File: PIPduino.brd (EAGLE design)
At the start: 46 x 46 mm, 41 parts, among them IC1 ATmega328P\, IC2 SPX1117, J1 ISP/SPI

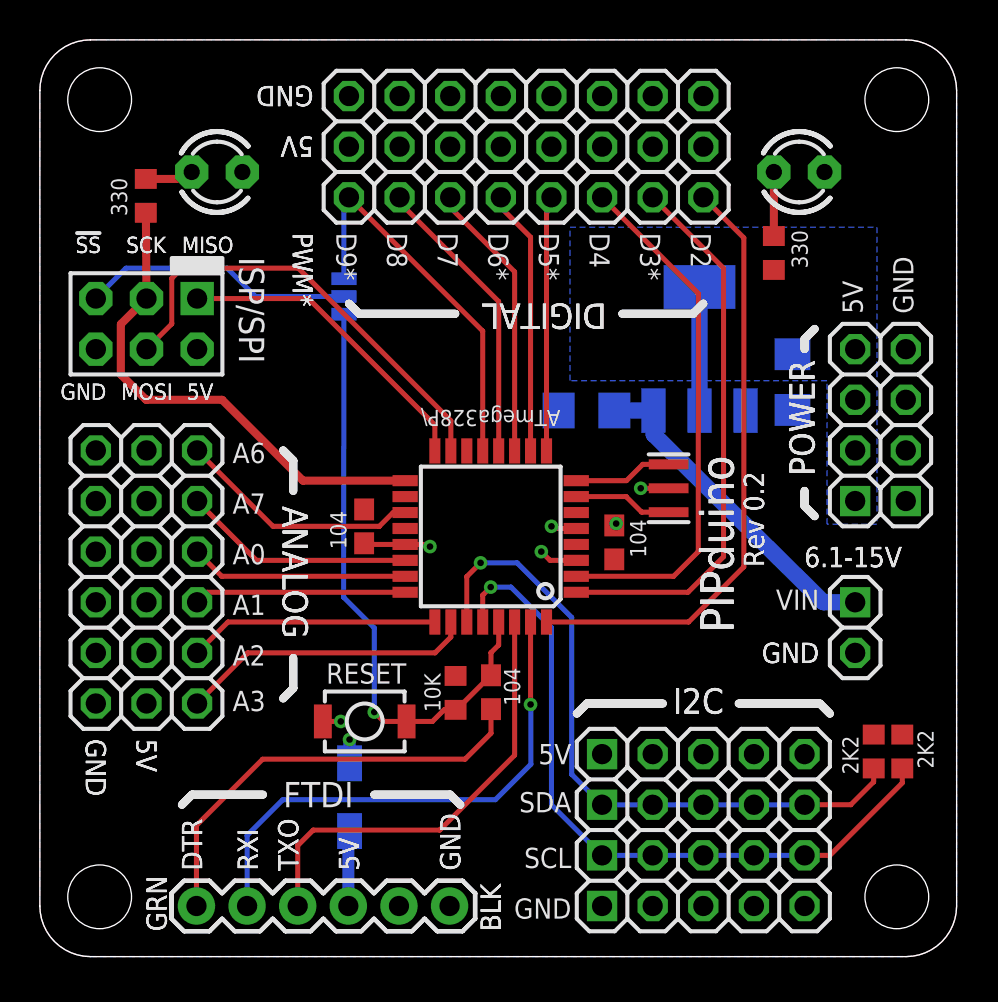
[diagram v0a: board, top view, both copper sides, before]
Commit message: Surrounded top screw holes with GND
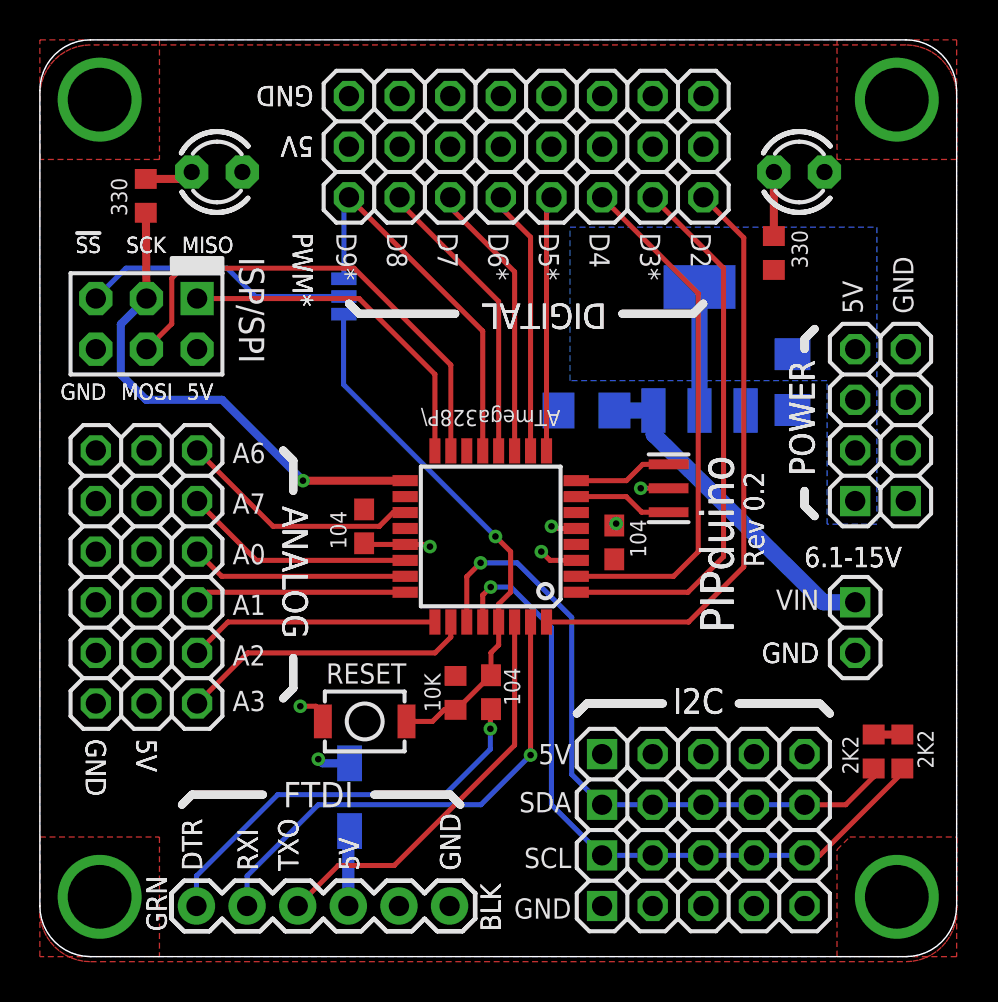
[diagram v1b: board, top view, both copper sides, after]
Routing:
- net !RESET: track 30.4 -> 27.2 mm
- net TXO: track 22.5 -> 20.4 mm
- net MOSI: track 23.0 -> 24.6 mm
- net 5V: track 7.76 -> 9.29 mm
- net MISO: track 15.9 -> 17.3 mm
- net RXI: track 26.4 -> 24.9 mm
- net N$15: track 22.0 -> 20.9 mm, vias 0 -> 1
- net GND: track 9.01 -> 9.81 mm, vias 6 -> 10
- net SCK: vias 0 -> 1
- added copper zone on layer 1, net GND

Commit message: Removed top 5V polygon, star pattern power, 106's on analog, 104 on aref, larger power traces, removed polygons on top mounting holes
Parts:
- added C6: 104, rcl:C0603
- added C7, C8: 106, rcl:C1206
- moved C5 2.08 mm to (29.0, 26.0), turned to 270 degrees
- moved C1 1.84 mm to (15.2, 23.1), turned to 180 degrees
- moved C3 0.60 mm to (29.4, 20.7), turned to 0 degrees
- moved C4 0.23 mm to (22.9, 13.2)
- moved R4 0.23 mm to (21.1, 13.2), turned to 270 degrees
- renumbered U$1 to X1
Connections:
- new net N$6: C6.1, IC1.20
- net 5V: now also C7.1, C8.1; no longer IC1.20
- net GND: now also C6.2, C7.2, C8.2
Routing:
- net 5V: track 9.29 -> 134.1 mm, vias 1 -> 5
- net N$6: track 0.00 -> 2.59 mm
- net !RESET: track 27.2 -> 27.9 mm
- net GND: track 9.81 -> 10.5 mm, vias 10 -> 12
- net A6: track 12.3 -> 11.8 mm, vias 0 -> 1
- net SCK: track 25.1 -> 25.4 mm, vias 1 -> 0
- removed copper zone on layer 1, net 5V
- removed copper zone on layer 1, net GND

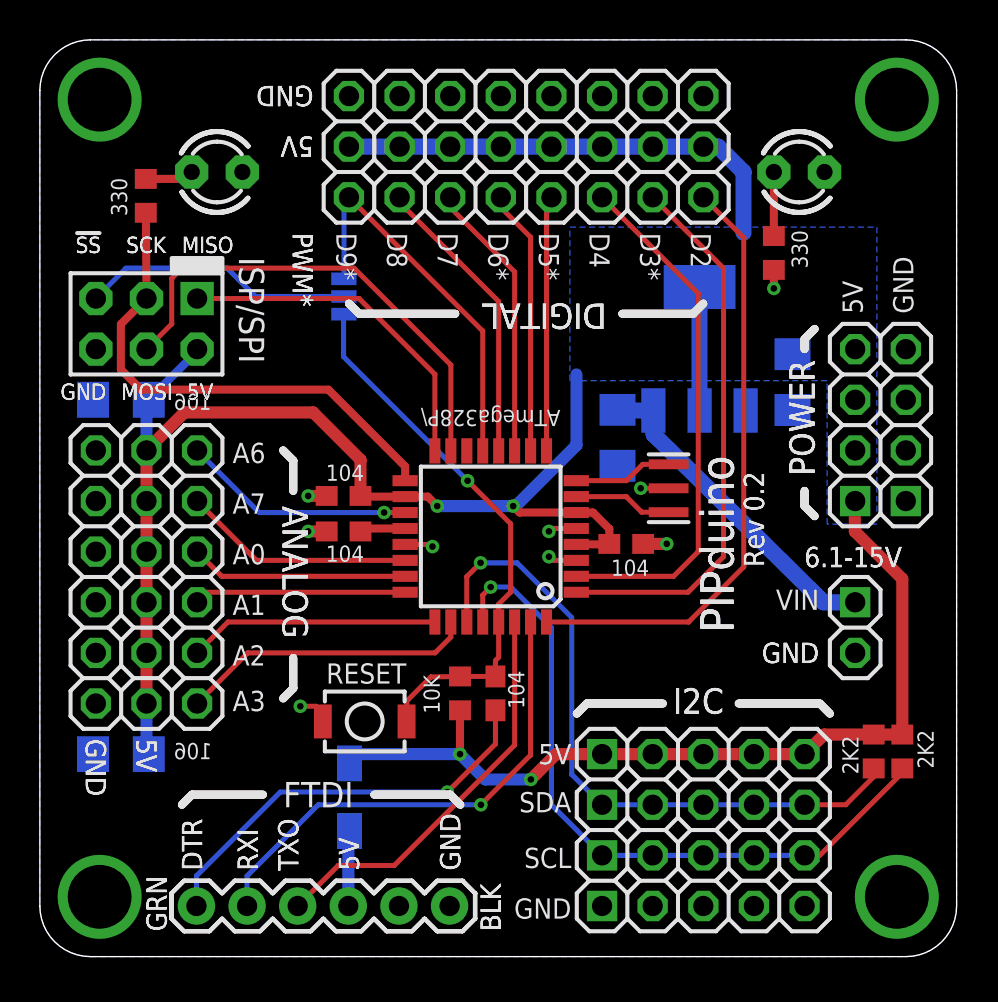
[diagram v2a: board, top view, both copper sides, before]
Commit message: Final LDO regulator selection, rearrangement, silk updates, fixed missing D10
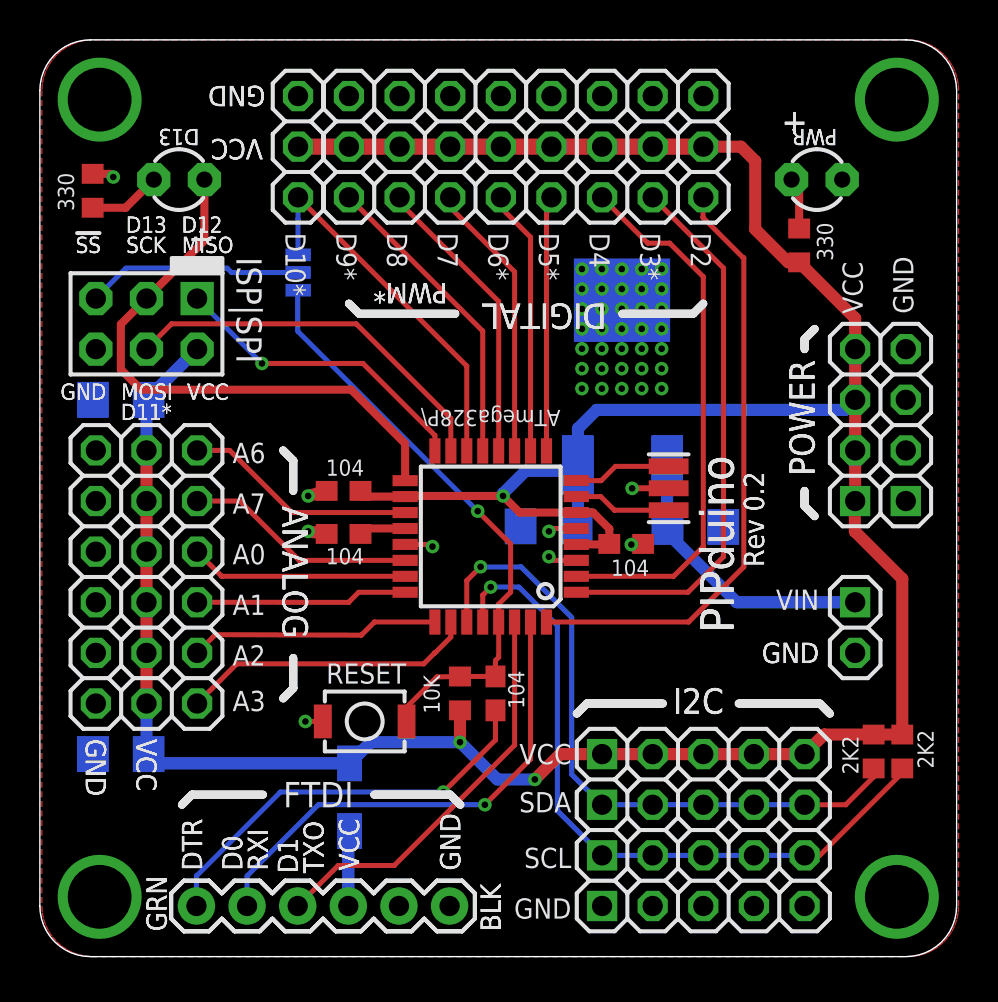
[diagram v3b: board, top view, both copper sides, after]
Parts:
- removed IC2: SPX1117, SparkFun:SOT223
- removed LED1, LED2: (no value), bt_opto:LED3MM
- added D13, PWR: (no value), bt_opto:LED3MM
- added JP2: D10*, pinhead-2:1X03-S
- added U1: NCP5500, bt_regulator:DPAK
- J1: value ISP/SPI -> ISP|SPI
- JP21, JP25: value 5V -> VCC
- moved C2 14.2 mm to (25.5, 21.6), turned to 0 degrees
- moved C5 5.94 mm to (32.9, 21.6), turned to 180 degrees
- moved R3 2.68 mm to (2.65, 38.4)
- moved SJ1 2.59 mm to (13.0, 34.3)
- moved R5 1.33 mm to (38.1, 35.7)
- moved C1 0.25 mm to (15.2, 23.4)
- moved C6 0.13 mm to (15.2, 21.2)
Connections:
- removed net !CS: IC1.14
- removed net 5V: C1.1, C2.1, C3.1, C7.1, C8.1, D1.C, IC1.18, IC1.4, IC1.6, IC2.2, IC2.4, J1.2, JP10.2, JP11.2, JP12.2, JP13.2, JP14.2, JP15.2, JP16.2, JP17.2, JP18.2, JP19.2, JP21.1, JP21.2, JP21.3, JP21.4, JP25.1, JP25.2, JP25.3, JP25.4, JP25.5, JP6.2, JP7.2, JP8.2, JP9.2, R1.2, R2.2, R4.2, R5.2
- new net D10: IC1.14, JP2.1, SJ1.3
- new net VCC: C1.1, C2.1, C3.1, C7.1, C8.1, D1.C, IC1.18, IC1.4, IC1.6, J1.2, JP10.2, JP11.2, JP12.2, JP13.2, JP14.2, JP15.2, JP16.2, JP17.2, JP18.2, JP19.2, JP2.2, JP21.1, JP21.2, JP21.3, JP21.4, JP25.1, JP25.2, JP25.3, JP25.4, JP25.5, JP6.2, JP7.2, JP8.2, JP9.2, R1.2, R2.2, R4.2, R5.2, U1.3
- net D9: no longer SJ1.3
- net GND: now also JP2.3, PWR.K, R3.1, U1.4; no longer IC2.1, LED1.K, LED2.K
- net N$1: now also D13.K, R3.2; no longer LED1.A, R3.1
- net N$2: now also U1.1; no longer IC2.3
- net N$4: now also PWR.A; no longer LED2.A
- net SCK: now also D13.A; no longer R3.2
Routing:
- net VCC: track 0.00 -> 158.9 mm, vias 0 -> 3
- net 5V: track 134.1 -> 0.00 mm, vias 5 -> 0
- net D10: track 0.00 -> 19.1 mm
- net MOSI: track 24.6 -> 19.4 mm
- net D9: track 19.7 -> 15.5 mm
- net SCK: track 25.4 -> 28.9 mm
- net N$3: track 13.7 -> 10.9 mm
- net N$2: track 16.7 -> 14.3 mm
- net !RESET: track 27.9 -> 29.9 mm
- net MISO: track 17.3 -> 15.6 mm, vias 0 -> 1
- net N$1: track 2.45 -> 3.65 mm
- net GND: track 10.5 -> 11.3 mm, vias 12 -> 48
- net D4: track 26.4 -> 27.3 mm
- net N$4: track 3.21 -> 2.61 mm
- net A6: track 11.8 -> 11.7 mm, vias 1 -> 0
- added copper zone on layer 1, net GND
- removed copper zone on layer 16, net 5V
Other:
- board text added: "+"
- board text added: "16MHz"
- board text added: "20MHz"
- board text added: "3.3V"
- board text added: "8MHz"
- board text added: "D0"
- board text added: "D10*"
- board text added: "D11*"
- board text added: "D12"
- board text added: "D13"
- board text added: "ISP|SPI"
- board text added: "NCP5500"
- board text added: "PWR"
- board text added: "VCC"
- board text added: "bot-thoughts.com"
- board text added: "http://is.gd/pipduino"
- board text removed: "6.1-15V"
- board text removed: "ISP/SPI"
- board text removed: "OUT=5V, 0.8A"
- board text removed: "SPX1117"
- board text removed: "www.bot-thoughts.com"
